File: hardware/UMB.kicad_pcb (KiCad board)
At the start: 2 copper layers, 162 parts, among them J1 PH1-03-UA, J10 PinHeader 02x04, J11 PinHeader 02x04, J12 PH1-03-UA, J13 Conn_01x05, J14 Conn_01x05, J15 FTSH-107-01-L-D-K, J16 Conn_01x05, J17 Conn_01x05, J18 Conn_01x05, J19 Conn_01x05, J2 PinHeader 02x04, J20 Conn_01x03, J21 Conn_01x03, J22 Conn_01x02, J23 Conn_01x02, J24 Conn_01x03, J25 Conn_01x03, J26 Conn_01x03, J27 Conn_01x03, J3 PinHeader 02x04, J4 PH1-03-UA, J5 PH1-03-UA, J6 PinHeader 02x04, J7 PinHeader 02x04, J8 PH1-03-UA, J9 PH1-03-UA, U1 STM32G0C1KCTxN, U10 TLV743P, U11 TLC274AIDR, U12 INA2128UA_1K, U13 TLC274AIDR, U14 TLC274AIDR, U15 INA2128UA_1K, U16 INA2128UA_1K, U2 ADS114S08BIPBSR, U3 ADM3057ExRW, U4 TPS563300DRLR, U5 TPS563219ADDFR, U6 AP2127N3-1.5, U7 LDK320ADU120R, U8 LM2940SX-12_NOPB, U9 LM1117IMP-5.0

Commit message: Preliminary components placement
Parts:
- removed TP1: TestPoint_Small, TestPoint:TestPoint_Pad_D1.0mm
- added H1: MountingHole_Pad, MountingHole:MountingHole_3.2mm_M3_Pad_TopBottom, F.Cu at (91.2, 177.3)
- added H2: MountingHole_Pad, MountingHole:MountingHole_3.2mm_M3_Pad_TopBottom, F.Cu at (91.2, 30.7)
- added H3: MountingHole_Pad, MountingHole:MountingHole_3.2mm_M3_Pad_TopBottom, F.Cu at (167.9, 30.7)
- added H4: MountingHole_Pad, MountingHole:MountingHole_3.2mm_M3_Pad_TopBottom, F.Cu at (167.9, 177.3)
- C14, C20: value 100n -> 10u; footprint Capacitor_SMD:C_0603_1608Metric_Pad1.08x0.95mm_HandSolder -> 10uFpolarized_cap:CAPAE660X600N
- C16: value 10u -> 100n; footprint 10uFpolarized_cap:CAPAE660X600N -> Capacitor_SMD:C_0603_1608Metric_Pad1.08x0.95mm_HandSolder
- C21: value 10u -> 8.2n; footprint 10uFpolarized_cap:CAPAE660X600N -> Capacitor_SMD:C_0603_1608Metric_Pad1.08x0.95mm_HandSolder
- C22: value 22u -> 100n
- C23: value 10u -> 22u; footprint 10uFpolarized_cap:CAPAE660X600N -> Capacitor_SMD:C_0603_1608Metric_Pad1.08x0.95mm_HandSolder
- C24: value 8.2n -> 10u; footprint Capacitor_SMD:C_0603_1608Metric_Pad1.08x0.95mm_HandSolder -> 10uFpolarized_cap:CAPAE660X600N
- C25: value 2.2u -> 470n; footprint Capacitor_SMD:C_0805_2012Metric_Pad1.18x1.45mm_HandSolder -> Capacitor_SMD:C_0603_1608Metric_Pad1.08x0.95mm_HandSolder
- C26: value 10u -> 22u; footprint Capacitor_SMD:C_0805_2012Metric_Pad1.18x1.45mm_HandSolder -> Capacitor_SMD:C_0603_1608Metric_Pad1.08x0.95mm_HandSolder
- C27: value 2.2u -> 10u
- C28: value 2.2u -> 22u; footprint Capacitor_SMD:C_0805_2012Metric_Pad1.18x1.45mm_HandSolder -> Capacitor_SMD:C_0603_1608Metric_Pad1.08x0.95mm_HandSolder
- C29: value 2.2u -> 1u; footprint Capacitor_SMD:C_0805_2012Metric_Pad1.18x1.45mm_HandSolder -> Capacitor_SMD:C_0603_1608Metric_Pad1.08x0.95mm_HandSolder
- C30: value 470n -> 100n
- C31: value 22u -> 1u
- C32: value 10u -> 2.2u
- C33: value 22u -> 10u; footprint Capacitor_SMD:C_0603_1608Metric_Pad1.08x0.95mm_HandSolder -> Capacitor_SMD:C_0805_2012Metric_Pad1.18x1.45mm_HandSolder
- C34, C36: value 1u -> 2.2u; footprint Capacitor_SMD:C_0603_1608Metric_Pad1.08x0.95mm_HandSolder -> Capacitor_SMD:C_0805_2012Metric_Pad1.18x1.45mm_HandSolder
- C35: value 100n -> 2.2u; footprint Capacitor_SMD:C_0603_1608Metric_Pad1.08x0.95mm_HandSolder -> Capacitor_SMD:C_0805_2012Metric_Pad1.18x1.45mm_HandSolder
- C6: value 100n -> 47u; footprint Capacitor_SMD:C_0603_1608Metric_Pad1.08x0.95mm_HandSolder -> Capacitor_SMD:C_0805_2012Metric_Pad1.18x1.45mm_HandSolder
- C7: value 47u -> 100n; footprint Capacitor_SMD:C_0805_2012Metric_Pad1.18x1.45mm_HandSolder -> Capacitor_SMD:C_0603_1608Metric_Pad1.08x0.95mm_HandSolder
- D13, D14: value SZESD9101P2T5G -> PESD5V0L2BT; footprint Diode_SMD:D_SOD-923 -> Package_TO_SOT_SMD:SOT-23_Handsoldering
- D15: value SZESD9101P2T5G -> 3.6V/400W; footprint Diode_SMD:D_SOD-923 -> Package_TO_SOT_SMD:SOT-23-6
- D5: value PESD5V0L2BT -> PESD12VL2BT,215
- D6: value 3.6V/400W -> PESD12VL2BT,215; footprint Package_TO_SOT_SMD:SOT-23-6 -> Package_TO_SOT_SMD:SOT-23_Handsoldering
- D7, D8: value PESD12VL2BT,215 -> SZESD9101P2T5G; footprint Package_TO_SOT_SMD:SOT-23_Handsoldering -> Diode_SMD:D_SOD-923
- D9: value PESD5V0L2BT -> SZESD9101P2T5G; footprint Package_TO_SOT_SMD:SOT-23_Handsoldering -> Diode_SMD:D_SOD-923
- J1, J4, J5: value PH1-03-UA -> PinHeader 02x04; footprint Connector_PinHeader_2.54mm:PinHeader_1x03_P2.54mm_Vertical -> Connector_PinHeader_2.54mm:PinHeader_2x04_P2.54mm_Vertical
- J10, J11, J7: value PinHeader 02x04 -> PH1-03-UA; footprint Connector_PinHeader_2.54mm:PinHeader_2x04_P2.54mm_Vertical -> Connector_PinHeader_2.54mm:PinHeader_1x03_P2.54mm_Vertical
- J15: value FTSH-107-01-L-D-K -> Conn_01x05; footprint Samacsys:FTSH-107-XX-YYY-D-K -> Wago_01x05:26011105
- J19: value Conn_01x05 -> Conn_01x03; footprint Wago_01x05:26011105 -> Wago_01x03:26011103
- J22, J23: value Conn_01x02 -> Conn_01x03; footprint Wago_01x02:26011102 -> Wago_01x03:26011103
- J25, J26: value Conn_01x03 -> Conn_01x02; footprint Wago_01x03:26011103 -> Wago_01x02:26011102
- J27: value Conn_01x03 -> FTSH-107-01-L-D-K; footprint Wago_01x03:26011103 -> Samacsys:FTSH-107-XX-YYY-D-K
- R14, R22: value 14k -> 12.4k
- R15, R35: value 12.4k -> 2.1k
- R16: value 2.1k -> 499R
- R17: value 499R -> 49.9R
- R18, R26: value 0R -> 12.4k
- R19: value 49.9R -> 2.1k
- R20: value 10k -> 499R
- R21, R29: value 12.4k -> 49.9R
- R27: value 10k -> 2.1k
- R28, R36: value 14k -> 499R
- R30: value 2.1k -> 12.4k
- R31: value 499R -> 2.1k
- R32: value 0R -> 499R
- R34: value 10k -> 12.4k
- R37: value 2.1k -> 49.9R
- R38: value 499R -> 14k
- R39: value 49.9R -> 0R
- R40, R46: value 0R -> 10k
- R41: value 10k -> 14k
- R42: value 14k -> 0R
- R43, R49: value 12.4k -> 10k
- R44: value 2.1k -> 14k
- R45: value 499R -> 0R
- R47, R53: value 49.9R -> 14k
- R48: value 10k -> 0R
- R51: value 2.1k -> 0R
- R52: value 499R -> 10k
- U10: value TLV743P -> LDK320ADU120R; footprint Package_TO_SOT_SMD:SOT-23-5 -> Package_TO_SOT_SMD:SOT-89-3_Handsoldering
- U11, U13: value TLC274AIDR -> INA2128UA_1K; footprint SOIC-14:SOIC127P600X175-14N -> difopamp:SOIC127P1030X265-16N
- U15, U16: value INA2128UA_1K -> TLC274AIDR; footprint difopamp:SOIC127P1030X265-16N -> SOIC-14:SOIC127P600X175-14N
- U6: value AP2127N3-1.5 -> LM2940SX-12_NOPB; footprint Package_TO_SOT_SMD:TSOT-23_HandSoldering -> DDPAK:KTT0003B
- U7: value LDK320ADU120R -> LM1117IMP-5.0; footprint Package_TO_SOT_SMD:SOT-89-3_Handsoldering -> Package_TO_SOT_SMD:SOT-223-3_TabPin2
- U8: value LM2940SX-12_NOPB -> TLV743P; footprint DDPAK:KTT0003B -> Package_TO_SOT_SMD:SOT-23-5
- U9: value LM1117IMP-5.0 -> AP2127N3-1.5; footprint Package_TO_SOT_SMD:SOT-223-3_TabPin2 -> Package_TO_SOT_SMD:TSOT-23_HandSoldering
- moved J6 164.1 mm to (110.8, 171.6), turned to 90 degrees
- moved J12 155.1 mm to (118.4, 162.7), turned to 180 degrees
- moved J11 152.6 mm to (139.7, 162.7), turned to 180 degrees
- moved J5 143.2 mm to (139.7, 171.6), turned to 90 degrees
- moved J10 140.9 mm to (118.6, 138.3), turned to 180 degrees
- moved R34 136.5 mm to (109.8, 176.9), turned to -90 degrees
- moved J4 136.1 mm to (110.9, 146.9), turned to 90 degrees
- moved R35 132.4 mm to (113.1, 176.9), turned to -90 degrees
- moved R53 131.9 mm to (112.6, 161.7)
- moved U13 130.0 mm to (129.1, 161.4), turned to 180 degrees
- moved J13 128.6 mm to (156.7, 124.7), turned to 90 degrees
- moved R36 128.3 mm to (116.4, 176.9), turned to -90 degrees
- moved R54 127.7 mm to (112.6, 157.6), turned to 180 degrees
- moved C13 127.7 mm to (111.7, 42.4), turned to 180 degrees
- moved R55 127.4 mm to (112.6, 159.6)
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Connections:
- C14 pad 1: Net-(U4-SW) -> +24V
- C14 pad 2: Net-(U4-BST) -> GND
- C16 pad 1: +24V -> Net-(U4-SW)
- C16 pad 2: GND -> Net-(U4-BST)
- C19 pad 1: Net-(U5-VBST) -> +14.5V
- C19 pad 2: Net-(U5-SW) -> GND
- C2 pad 1: +5V -> +5VA
- C2 pad 2: GND -> AGND
- C21 pad 1: +14.5V -> Net-(U5-SS)
- C22 pad 1: +7V -> Net-(U5-VBST)
- C22 pad 2: GND -> Net-(U5-SW)
- C24 pad 1: Net-(U5-SS) -> +7V
- C25 pad 1: +7V -> +14.5V
- C25 pad 2: AGND -> GND
- C26 pad 1: +5VA -> +12V
- C26 pad 2: AGND -> GND
- C27 pad 1: +5VA -> +7V
- C27 pad 2: AGND -> GND
- C28 pad 1: +14.5V -> +5V
- C28 pad 2: AGND -> GND
- C29 pad 1: +12VA -> +7V
- C29 pad 2: AGND -> GND
- C3 pad 1: GND -> AGND
- C30 pad 1: +14.5V -> +3.3V
- C31 pad 1: +12V -> +3.3V
- C33 pad 1: +5V -> +5VA
- C33 pad 2: GND -> AGND
- C34 pad 1: +7V -> +5VA
- C34 pad 2: GND -> AGND
- C35 pad 1: +3.3V -> +14.5V
- C36 pad 1: +3.3V -> +12VA
- C36 pad 2: GND -> AGND
- C39 pad 1: +5V -> AGND
- C39 pad 2: AGND -> +12VA
- C40 pad 1: +5V -> +5VA
- C41 pad 1: +5V -> +5VA
- C42 pad 1: AGND -> +5VA
- C42 pad 2: +12VA -> AGND
- C6 pad 1: +3.3V -> GND
- C6 pad 2: GND -> Net-(U3-VCC)
- C7 pad 1: GND -> +3.3V
- C7 pad 2: Net-(U3-VCC) -> GND
- D1 pad 1: /Analog/DIF1+ -> /Analog/DIF1-
- D1 pad 2: /Analog/DIF1- -> /Analog/DIF1+
- D10 pad 1: SE1IN -> SE4IN
- D11 pad 1: SE4IN -> SE5IN
- D12 pad 1: SE2IN -> SE6IN
- D13 pad 1: SE5IN -> /CAN/CAN+
- D13 pad 2: GND -> /CAN/CAN-
- D14 pad 1: SE3IN -> /Connectors/UART_RX
- D14 pad 2: GND -> /Connectors/UART_TX
- D15 pad 1: SE6IN -> /Connectors/NRST
- D2 pad 1: /Analog/DIF4+ -> /Analog/DIF2+
- D2 pad 2: /Analog/DIF4- -> /Analog/DIF2-
- D3 pad 1: /Analog/DIF2+ -> /Analog/DIF3-
- D3 pad 2: /Analog/DIF2- -> /Analog/DIF3+
- D4 pad 1: /Analog/DIF5+ -> /Analog/DIF4+
- D4 pad 2: /Analog/DIF5- -> /Analog/DIF4-
- D5 pad 1: /Connectors/UART_RX -> /Analog/DIF5-
- D5 pad 2: /Connectors/UART_TX -> /Analog/DIF5+
- D6 pad 1: /Connectors/NRST -> /Analog/DIF6+
- D6 pad 2: GND -> /Analog/DIF6-
- D6 pad 3: /Connectors/SWO -> GND
- D7 pad 1: /Analog/DIF3+ -> SE1IN
- D7 pad 2: /Analog/DIF3- -> GND
- D8 pad 1: /Analog/DIF6+ -> SE2IN
- D8 pad 2: /Analog/DIF6- -> GND
- D9 pad 1: /CAN/CAN+ -> SE3IN
- D9 pad 2: /CAN/CAN- -> GND
- J1 pad 2: /Analog/DIF1_12 -> /Analog/RGA1_2
- J1 pad 3: Net-(J1-Pin_3) -> Net-(J1-Pin_2)
- J10 pad 2: Net-(J10-Pin_2) -> /Analog/DIF4_12
- J11 pad 2: Net-(J11-Pin_2) -> /Analog/DIF5_12
- J14 pad 2: /Analog/DIF4- -> /Analog/DIF2-
- J14 pad 3: /Analog/DIF4+ -> /Analog/DIF2+
- J15 pad 1: unconnected-(J15-Pin_1-Pad1) -> GND
- J15 pad 2: unconnected-(J15-Pin_2-Pad2) -> /Analog/DIF3-
- J15 pad 3: +3.3V -> /Analog/DIF3+
- J15 pad 4: /Connectors/SWDIO -> +5V
- J15 pad 5: GND -> +12V
- J16 pad 2: /Analog/DIF2- -> /Analog/DIF4-
- J16 pad 3: /Analog/DIF2+ -> /Analog/DIF4+
- J18 pad 2: /Analog/DIF3- -> /Analog/DIF6-
- J18 pad 3: /Analog/DIF3+ -> /Analog/DIF6+
- J19 pad 2: /Analog/DIF6- -> SE1IN
- J19 pad 3: /Analog/DIF6+ -> +5V
- J2 pad 2: Net-(J2-Pin_2) -> /Analog/RGA2_2
- J2 pad 3: Net-(J2-Pin_3) -> Net-(J2-Pin_2)
- J2 pad 4: Net-(J2-Pin_4) -> /Analog/RGA2_2
- J2 pad 5: /Analog/RGA1_2 -> Net-(J2-Pin_3)
- J2 pad 6: /Analog/RGA1_2 -> /Analog/RGA2_2
- J2 pad 7: /Analog/RGA1_2 -> Net-(J2-Pin_4)
- J2 pad 8: /Analog/RGA1_2 -> /Analog/RGA2_2
- J20 pad 2: SE1IN -> SE2IN
- J21 pad 2: SE4IN -> SE3IN
- J22 pad 1: /CAN/CAN+ -> GND
- J22 pad 2: /CAN/CAN- -> SE4IN
- J23 pad 2: +24V -> SE5IN
- J24 pad 2: SE2IN -> SE6IN
- J25 pad 1: GND -> /CAN/CAN-
- J25 pad 2: SE5IN -> /CAN/CAN+
- J26 pad 1: GND -> +24V
- J26 pad 2: SE3IN -> GND
- J27 pad 1: GND -> unconnected-(J27-Pin_1-Pad1)
- J27 pad 2: SE6IN -> unconnected-(J27-Pin_2-Pad2)
- J27 pad 3: +5V -> +3.3V
- J3 pad 2: Net-(J3-Pin_2) -> /Analog/RGA3_2
- J3 pad 3: Net-(J3-Pin_3) -> Net-(J3-Pin_2)
- J3 pad 4: Net-(J3-Pin_4) -> /Analog/RGA3_2
- J3 pad 5: /Analog/RGA2_2 -> Net-(J3-Pin_3)
- J3 pad 6: /Analog/RGA2_2 -> /Analog/RGA3_2
- J3 pad 7: /Analog/RGA2_2 -> Net-(J3-Pin_4)
- J3 pad 8: /Analog/RGA2_2 -> /Analog/RGA3_2
- J4 pad 2: /Analog/DIF2_12 -> /Analog/RGA4_2
- J4 pad 3: Net-(J4-Pin_3) -> Net-(J4-Pin_2)
- J5 pad 2: /Analog/DIF3_12 -> /Analog/RGA5_2
- J5 pad 3: Net-(J5-Pin_3) -> Net-(J5-Pin_2)
- J6 pad 2: Net-(J6-Pin_2) -> /Analog/RGA6_2
- J6 pad 3: Net-(J6-Pin_3) -> Net-(J6-Pin_2)
- J6 pad 4: Net-(J6-Pin_4) -> /Analog/RGA6_2
- J6 pad 5: /Analog/RGA3_2 -> Net-(J6-Pin_3)
- J6 pad 6: /Analog/RGA3_2 -> /Analog/RGA6_2
- J6 pad 7: /Analog/RGA3_2 -> Net-(J6-Pin_4)
- J6 pad 8: /Analog/RGA3_2 -> /Analog/RGA6_2
- J7 pad 2: Net-(J7-Pin_2) -> /Analog/DIF1_12
- J8 pad 2: /Analog/DIF4_12 -> /Analog/DIF2_12
- J9 pad 2: /Analog/DIF5_12 -> /Analog/DIF3_12
- R14 pad 1: Net-(U11C--) -> Net-(J1-Pin_1)
- R14 pad 2: Net-(J1-Pin_1) -> /Analog/RGA1_1
- R15 pad 1: Net-(J2-Pin_1) -> Net-(J1-Pin_2)
- R16 pad 1: Net-(J2-Pin_2) -> Net-(J1-Pin_3)
- R17 pad 1: Net-(J2-Pin_3) -> Net-(J1-Pin_4)
- R18 pad 1: Net-(J1-Pin_3) -> Net-(J2-Pin_1)
- R18 pad 2: Net-(U11C--) -> /Analog/RGA2_1
- R19 pad 1: Net-(J2-Pin_4) -> Net-(J2-Pin_2)
- R19 pad 2: /Analog/RGA1_1 -> /Analog/RGA2_1
- R20 pad 1: Net-(U11C--) -> Net-(J2-Pin_3)
- R20 pad 2: AGND -> /Analog/RGA2_1
- R21 pad 1: Net-(J3-Pin_1) -> Net-(J2-Pin_4)
- R22 pad 1: Net-(U11D--) -> Net-(J3-Pin_1)
- R22 pad 2: Net-(J4-Pin_1) -> /Analog/RGA3_1
- R23 pad 2: /Analog/RGA2_1 -> /Analog/RGA3_1
- R24 pad 2: /Analog/RGA2_1 -> /Analog/RGA3_1
- R25 pad 2: /Analog/RGA2_1 -> /Analog/RGA3_1
- R26 pad 1: Net-(J4-Pin_3) -> Net-(J4-Pin_1)
- R26 pad 2: Net-(U11D--) -> /Analog/RGA4_1
- R27 pad 1: Net-(U11D--) -> Net-(J4-Pin_2)
- R27 pad 2: AGND -> /Analog/RGA4_1
- R28 pad 1: Net-(U14A--) -> Net-(J4-Pin_3)
- R28 pad 2: Net-(J5-Pin_1) -> /Analog/RGA4_1
- R29 pad 1: Net-(J6-Pin_1) -> Net-(J4-Pin_4)
- R29 pad 2: /Analog/RGA3_1 -> /Analog/RGA4_1
- R30 pad 1: Net-(J6-Pin_2) -> Net-(J5-Pin_1)
- R30 pad 2: /Analog/RGA3_1 -> /Analog/RGA5_1
- R31 pad 1: Net-(J6-Pin_3) -> Net-(J5-Pin_2)
- R31 pad 2: /Analog/RGA3_1 -> /Analog/RGA5_1
- R32 pad 2: Net-(U14A--) -> /Analog/RGA5_1
- R33 pad 1: Net-(J6-Pin_4) -> Net-(J5-Pin_4)
- R33 pad 2: /Analog/RGA3_1 -> /Analog/RGA5_1
- R34 pad 1: Net-(U14A--) -> Net-(J6-Pin_1)
- R34 pad 2: AGND -> /Analog/RGA6_1
- R35 pad 1: Net-(J7-Pin_1) -> Net-(J6-Pin_2)
- R35 pad 2: /Analog/RGA4_1 -> /Analog/RGA6_1
- R36 pad 1: Net-(U14B--) -> Net-(J6-Pin_3)
- R36 pad 2: Net-(J8-Pin_1) -> /Analog/RGA6_1
- R37 pad 1: Net-(J7-Pin_2) -> Net-(J6-Pin_4)
- R37 pad 2: /Analog/RGA4_1 -> /Analog/RGA6_1
- R38 pad 1: Net-(J7-Pin_3) -> Net-(U16C--)
- R38 pad 2: /Analog/RGA4_1 -> Net-(J7-Pin_1)
- R39 pad 1: Net-(J7-Pin_4) -> Net-(J7-Pin_3)
- R39 pad 2: /Analog/RGA4_1 -> Net-(U16C--)
- R4 pad 1: Net-(U1-PB0) -> Net-(U1-PA7)
- R4 pad 2: /ADC/ADC_DRDY -> /ADC/ADC_SPI.MOSI
- R40 pad 1: Net-(J8-Pin_3) -> Net-(U16C--)
- R40 pad 2: Net-(U14B--) -> AGND
- R41 pad 1: Net-(U14B--) -> Net-(U15D--)
- R41 pad 2: AGND -> Net-(J8-Pin_1)
- R42 pad 1: Net-(U14C--) -> Net-(J8-Pin_3)
- R42 pad 2: Net-(J9-Pin_1) -> Net-(U15D--)
- R43 pad 1: Net-(J10-Pin_1) -> Net-(U15D--)
- R43 pad 2: /Analog/RGA5_1 -> AGND
- R44 pad 1: Net-(J10-Pin_2) -> Net-(U14A--)
- R44 pad 2: /Analog/RGA5_1 -> Net-(J9-Pin_1)
- R45 pad 1: Net-(J10-Pin_3) -> Net-(J9-Pin_3)
- R45 pad 2: /Analog/RGA5_1 -> Net-(U14A--)
- R46 pad 1: Net-(J9-Pin_3) -> Net-(U14A--)
- R46 pad 2: Net-(U14C--) -> AGND
- R47 pad 1: Net-(J10-Pin_4) -> Net-(U14B--)
- R47 pad 2: /Analog/RGA5_1 -> Net-(J10-Pin_1)
- R48 pad 1: Net-(U14C--) -> Net-(J10-Pin_3)
- R48 pad 2: AGND -> Net-(U14B--)
- R49 pad 1: Net-(J11-Pin_1) -> Net-(U14B--)
- R49 pad 2: /Analog/RGA6_1 -> AGND
- R5 pad 1: Net-(U1-PA7) -> Net-(U1-PB0)
- R5 pad 2: /ADC/ADC_SPI.MOSI -> /ADC/ADC_DRDY
- R50 pad 2: Net-(J12-Pin_1) -> Net-(J11-Pin_1)
- R51 pad 1: Net-(J11-Pin_2) -> Net-(J11-Pin_3)
- R51 pad 2: /Analog/RGA6_1 -> Net-(U14D--)
- R52 pad 1: Net-(J11-Pin_3) -> Net-(U14D--)
- R52 pad 2: /Analog/RGA6_1 -> AGND
- R53 pad 1: Net-(J11-Pin_4) -> Net-(U14C--)
- R53 pad 2: /Analog/RGA6_1 -> Net-(J12-Pin_1)
- R54 pad 2: Net-(U14D--) -> Net-(U14C--)
- R55 pad 1: Net-(U14D--) -> Net-(U14C--)
- R8 pad 1: /CAN/GND_CAN_ISO -> Net-(U3-RS)
- R8 pad 2: Net-(U3-RS) -> /CAN/GND_CAN_ISO
- U10 pad 1: +7V -> +12VA
- U10 pad 2: GND -> AGND
- U10 pad 3: +7V -> +14.5V
- U11 pad 1: /ADC/SE5 -> /Analog/DIF1-
- U11 pad 10: /ADC/DIF1 -> /Analog/DIF2_12
- U11 pad 11: AGND -> /Analog/DIF2_12
- U11 pad 12: /ADC/DIF2 -> AGND
- U11 pad 13: Net-(U11D--) -> /Analog/RGA2_2
- U11 pad 14: /ADC/DIF2 -> /Analog/RGA2_1
- U11 pad 2: SE5IN -> /Analog/DIF1+
- U11 pad 3: /ADC/SE5 -> /Analog/RGA1_1
- U11 pad 4: +5V -> /Analog/RGA1_2
- U11 pad 5: /ADC/SE6 -> AGND
- U11 pad 6: SE6IN -> /Analog/DIF1_12
- U11 pad 7: /ADC/SE6 -> /Analog/DIF1_12
- U11 pad 8: /ADC/DIF1 -> AGND
- U11 pad 9: Net-(U11C--) -> +12VA
- U12 pad 1: /Analog/DIF1- -> /Analog/DIF3-
- U12 pad 10: /Analog/DIF2_12 -> /Analog/DIF4_12
- U12 pad 11: /Analog/DIF2_12 -> /Analog/DIF4_12
- U12 pad 13: /Analog/RGA2_2 -> /Analog/RGA4_2
- U12 pad 14: /Analog/RGA2_1 -> /Analog/RGA4_1
- U12 pad 15: /Analog/DIF2+ -> /Analog/DIF4+
- U12 pad 16: /Analog/DIF2- -> /Analog/DIF4-
- U12 pad 2: /Analog/DIF1+ -> /Analog/DIF3+
- U12 pad 3: /Analog/RGA1_1 -> /Analog/RGA3_1
- U12 pad 4: /Analog/RGA1_2 -> /Analog/RGA3_2
- U12 pad 6: /Analog/DIF1_12 -> /Analog/DIF3_12
- U12 pad 7: /Analog/DIF1_12 -> /Analog/DIF3_12
- U13 pad 1: /ADC/SE1 -> /Analog/DIF5-
- U13 pad 10: /ADC/SE3 -> /Analog/DIF6_12
- U13 pad 11: AGND -> /Analog/DIF6_12
- U13 pad 12: /ADC/SE4 -> AGND
- U13 pad 13: SE4IN -> /Analog/RGA6_2
- U13 pad 14: /ADC/SE4 -> /Analog/RGA6_1
- U13 pad 2: SE1IN -> /Analog/DIF5+
- U13 pad 3: /ADC/SE1 -> /Analog/RGA5_1
- U13 pad 4: +5V -> /Analog/RGA5_2
- U13 pad 5: /ADC/SE2 -> AGND
- U13 pad 6: SE2IN -> /Analog/DIF5_12
- U13 pad 7: /ADC/SE2 -> /Analog/DIF5_12
- U13 pad 8: /ADC/SE3 -> AGND
- U13 pad 9: SE3IN -> +12VA
- U14 pad 10: /ADC/DIF5 -> /ADC/DIF6
- U14 pad 12: /ADC/DIF6 -> /ADC/DIF5
- U14 pad 14: /ADC/DIF6 -> /ADC/DIF5
- U14 pad 4: +5V -> +5VA
- U14 pad 8: /ADC/DIF5 -> /ADC/DIF6
- U15 pad 1: /Analog/DIF3- -> /ADC/SE4
- U15 pad 10: /Analog/DIF4_12 -> /ADC/SE6
- U15 pad 11: /Analog/DIF4_12 -> AGND
- U15 pad 12: AGND -> /ADC/DIF2
- U15 pad 13: /Analog/RGA4_2 -> Net-(U15D--)
- U15 pad 14: /Analog/RGA4_1 -> /ADC/DIF2
- U15 pad 2: /Analog/DIF3+ -> SE4IN
- U15 pad 3: /Analog/RGA3_1 -> /ADC/SE4
- U15 pad 4: /Analog/RGA3_2 -> +5VA
- U15 pad 5: AGND -> /ADC/SE5
- U15 pad 6: /Analog/DIF3_12 -> SE5IN
- U15 pad 7: /Analog/DIF3_12 -> /ADC/SE5
- U15 pad 8: AGND -> /ADC/SE6
- U15 pad 9: +12VA -> SE6IN
- U16 pad 1: /Analog/DIF5- -> /ADC/SE2
- U16 pad 10: /Analog/DIF6_12 -> /ADC/DIF1
- U16 pad 11: /Analog/DIF6_12 -> AGND
- U16 pad 12: AGND -> /ADC/SE3
- U16 pad 13: /Analog/RGA6_2 -> SE3IN
- U16 pad 14: /Analog/RGA6_1 -> /ADC/SE3
- U16 pad 2: /Analog/DIF5+ -> SE2IN
- U16 pad 3: /Analog/RGA5_1 -> /ADC/SE2
- U16 pad 4: /Analog/RGA5_2 -> +5VA
- U16 pad 5: AGND -> /ADC/SE1
- U16 pad 6: /Analog/DIF5_12 -> SE1IN
- U16 pad 7: /Analog/DIF5_12 -> /ADC/SE1
- U16 pad 8: AGND -> /ADC/DIF1
- U16 pad 9: +12VA -> Net-(U16C--)
- U2 pad 24: GND -> AGND
- U2 pad 26: +5V -> +5VA
- U2 pad 27: GND -> AGND
- U2 pad 28: GND -> AGND
- U6 pad 1: AGND -> +14.5V
- U6 pad 2: +5VA -> GND
- U6 pad 3: +7V -> +12V
- U7 pad 1: +12VA -> GND
- U7 pad 2: AGND -> +5V
- U7 pad 3: +14.5V -> +7V
- U8 pad 1: +14.5V -> +7V
- U8 pad 3: +12V -> +7V
- U9 pad 1: GND -> AGND
- U9 pad 2: +5V -> +5VA
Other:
- board outline added: 84.8 x 154.7 mm
- copper layers 2 -> 6
- rule pad_to_mask_clearance: 0 -> 0.038

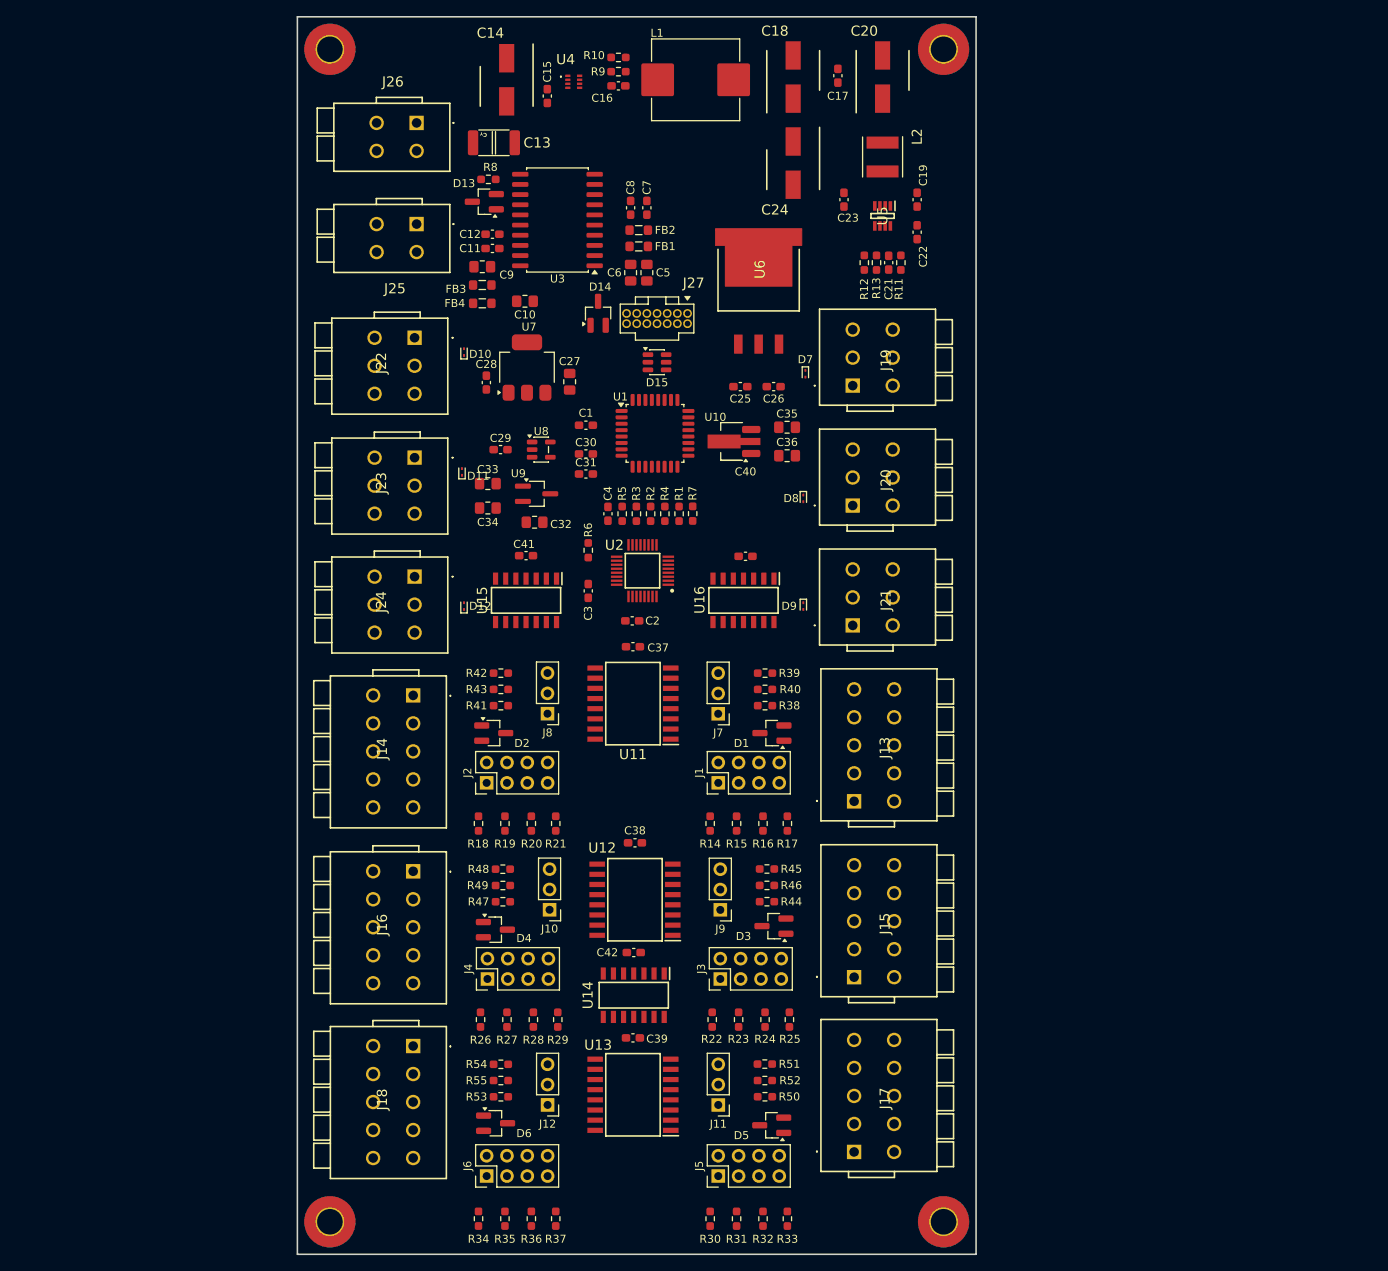
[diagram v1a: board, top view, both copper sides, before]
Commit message: Finished components placement on PCB
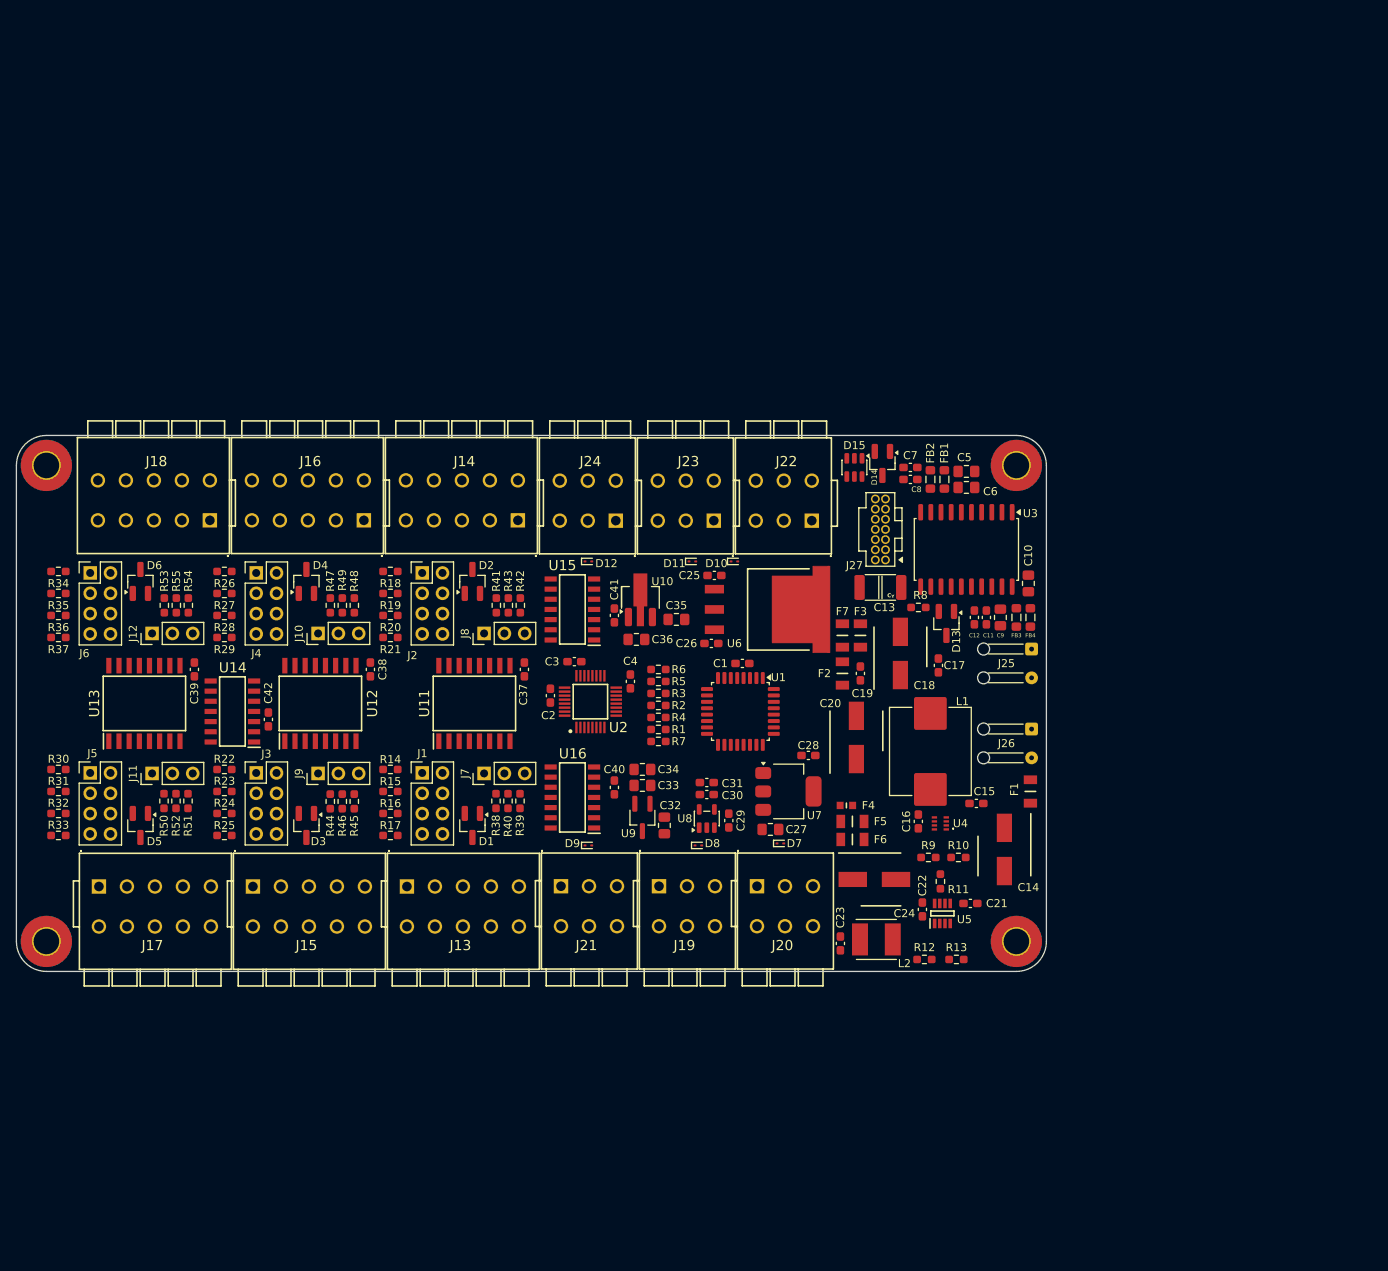
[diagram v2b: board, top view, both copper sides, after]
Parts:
- added F1: 3 A, fuse 1206:FUSC3215X66N, F.Cu at (178.8, 123.5)
- added F2: 3 A, fuse 1206:FUSC3215X66N, F.Cu at (155.2, 108.8)
- added F3: 1 A, fuse 1206:FUSC3215X66N, F.Cu at (157.5, 104.0)
- added F4: 800 mA, fuse 0603:FUSC1608X55N, F.Cu at (155.8, 125.2)
- added F5: 375 mA, fuse 1206:FUSC3215X66N, F.Cu at (156.5, 127.2)
- added F6: 375 mA, fuse 1206:FUSC3215X66N, F.Cu at (156.5, 129.5)
- added F7: 200 mA, fuse 1206:FUSC3215X66N, F.Cu at (155.2, 104.0)
- J25, J26: footprint Wago_01x02:26011102 -> StrainRelief:Wire_StrainRelief
- L2: footprint inductor:VLS5045EX330M -> inductor 68uh:VLS5045EX330M
- moved H4 117.5 mm to (55.8, 142.2), turned to -90 degrees
- moved C14 114.6 mm to (175.5, 130.8)
- moved H3 111.9 mm to (177.0, 142.2), turned to -90 degrees
- moved R10 108.7 mm to (169.8, 131.8)
- moved J26 107.0 mm to (175.8, 117.5)
- moved R9 105.6 mm to (166.0, 131.8), turned to 180 degrees
- moved C15 103.4 mm to (172.0, 125.0), turned to 0 degrees
- moved U4 103.4 mm to (167.5, 127.5), turned to 180 degrees
- moved R33 103.0 mm to (57.2, 129.0), turned to 180 degrees
- moved R32 101.6 mm to (57.2, 126.2), turned to 180 degrees
- moved H1 101.0 mm to (55.8, 82.8), turned to -90 degrees
- moved H2 100.3 mm to (177.0, 82.8), turned to -90 degrees
- moved R31 100.2 mm to (57.2, 123.5), turned to 180 degrees
- moved C16 99.3 mm to (164.7, 127.2), turned to -90 degrees
- moved R30 99.0 mm to (57.2, 120.8), turned to 180 degrees
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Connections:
- C14 pad 1: +24V -> Net-(U4-VIN)
- C15 pad 1: +24V -> Net-(U4-VIN)
- C19 pad 1: +14.5V -> Net-(U5-VIN)
- C20 pad 1: +14.5V -> Net-(U5-VIN)
- C25 pad 1: +14.5V -> Net-(U6-IN)
- C27 pad 1: +7V -> Net-(U7-VI)
- C29 pad 1: +7V -> Net-(U8-EN)
- C32 pad 1: +7V -> Net-(U9-VI)
- C35 pad 1: +14.5V -> Net-(U10-IN)
- J25 pad 1: /CAN/CAN- -> /CAN/CAN+
- J25 pad 2: /CAN/CAN+ -> /CAN/CAN-
- J26 pad 1: +24V -> GND
- J26 pad 2: GND -> +24V
- R11 pad 1: +14.5V -> Net-(U5-VIN)
- U10 pad 3: +14.5V -> Net-(U10-IN)
- U12 pad 1: /Analog/DIF3- -> /Analog/DIF3+
- U12 pad 2: /Analog/DIF3+ -> /Analog/DIF3-
- U4 pad 3: +24V -> Net-(U4-VIN)
- U5 pad 3: +14.5V -> Net-(U5-VIN)
- U6 pad 1: +14.5V -> Net-(U6-IN)
- U7 pad 3: +7V -> Net-(U7-VI)
- U8 pad 1: +7V -> Net-(U8-EN)
- U8 pad 3: +7V -> Net-(U8-EN)
- U9 pad 3: +7V -> Net-(U9-VI)
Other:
- board size 84.8 x 154.7 mm -> 128.8 x 67 mm
